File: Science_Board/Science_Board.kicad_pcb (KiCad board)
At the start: 2 copper layers, 217 x 149.5 mm, 136 parts, among them J1 Conn_01x02, J10 Conn_01x02, J11 Conn_01x03, J12 Conn_01x03, J13 Conn_01x03, J14 Conn_01x03, J15 Conn_01x03, J16 Conn_01x03, J17 Conn_01x03, J18 Conn_01x03, J19 Conn_01x02, J2 RJ45_LED_Shielded, J20 Molex_Megafit_02, J21 Molex_Megafit_02, J22 Molex_Megafit_02, J23 Conn_01x02, J3 Molex_Megafit_02, J4 Molex_Megafit_02, J5 Conn_01x05, J6 Conn_01x04, J7 Conn_01x03, J8 Conn_01x03, J9 Conn_01x02, Q1 BS250, Q2 NMOS, Q3 NMOS, Q4 NMOS, Q5 NMOS, SW1 SW_Push, SW10 SW_Push, SW11 SW_Push, SW12 SW_SPDT, SW2 SW_Push, SW3 SW_Push, SW4 SW_Push, SW5 SW_Push, SW6 SW_Push, SW7 SW_Push, SW8 SW_Push, SW9 SW_Push, U1 AP63205WU, U5 PCA9685BS

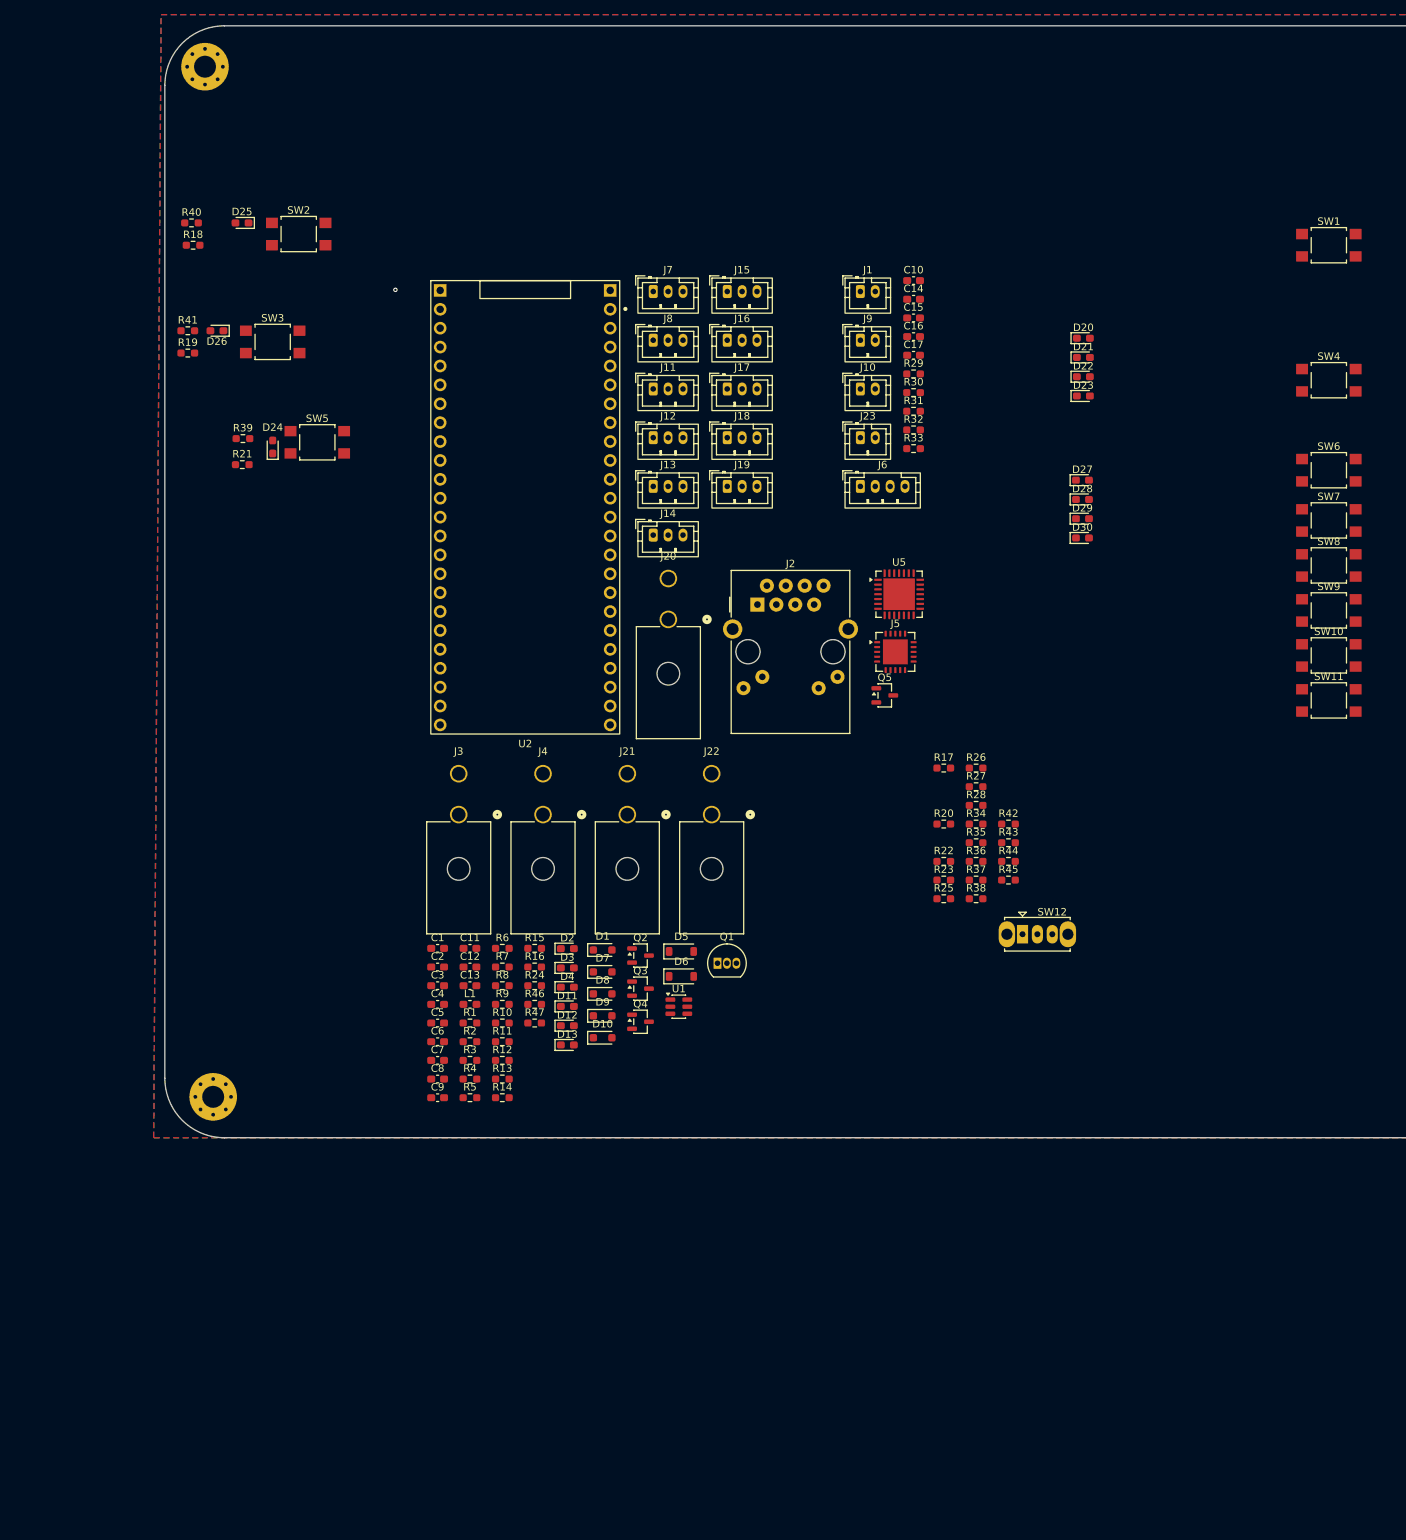
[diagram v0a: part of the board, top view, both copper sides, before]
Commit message: Got all the buttons close to eachother
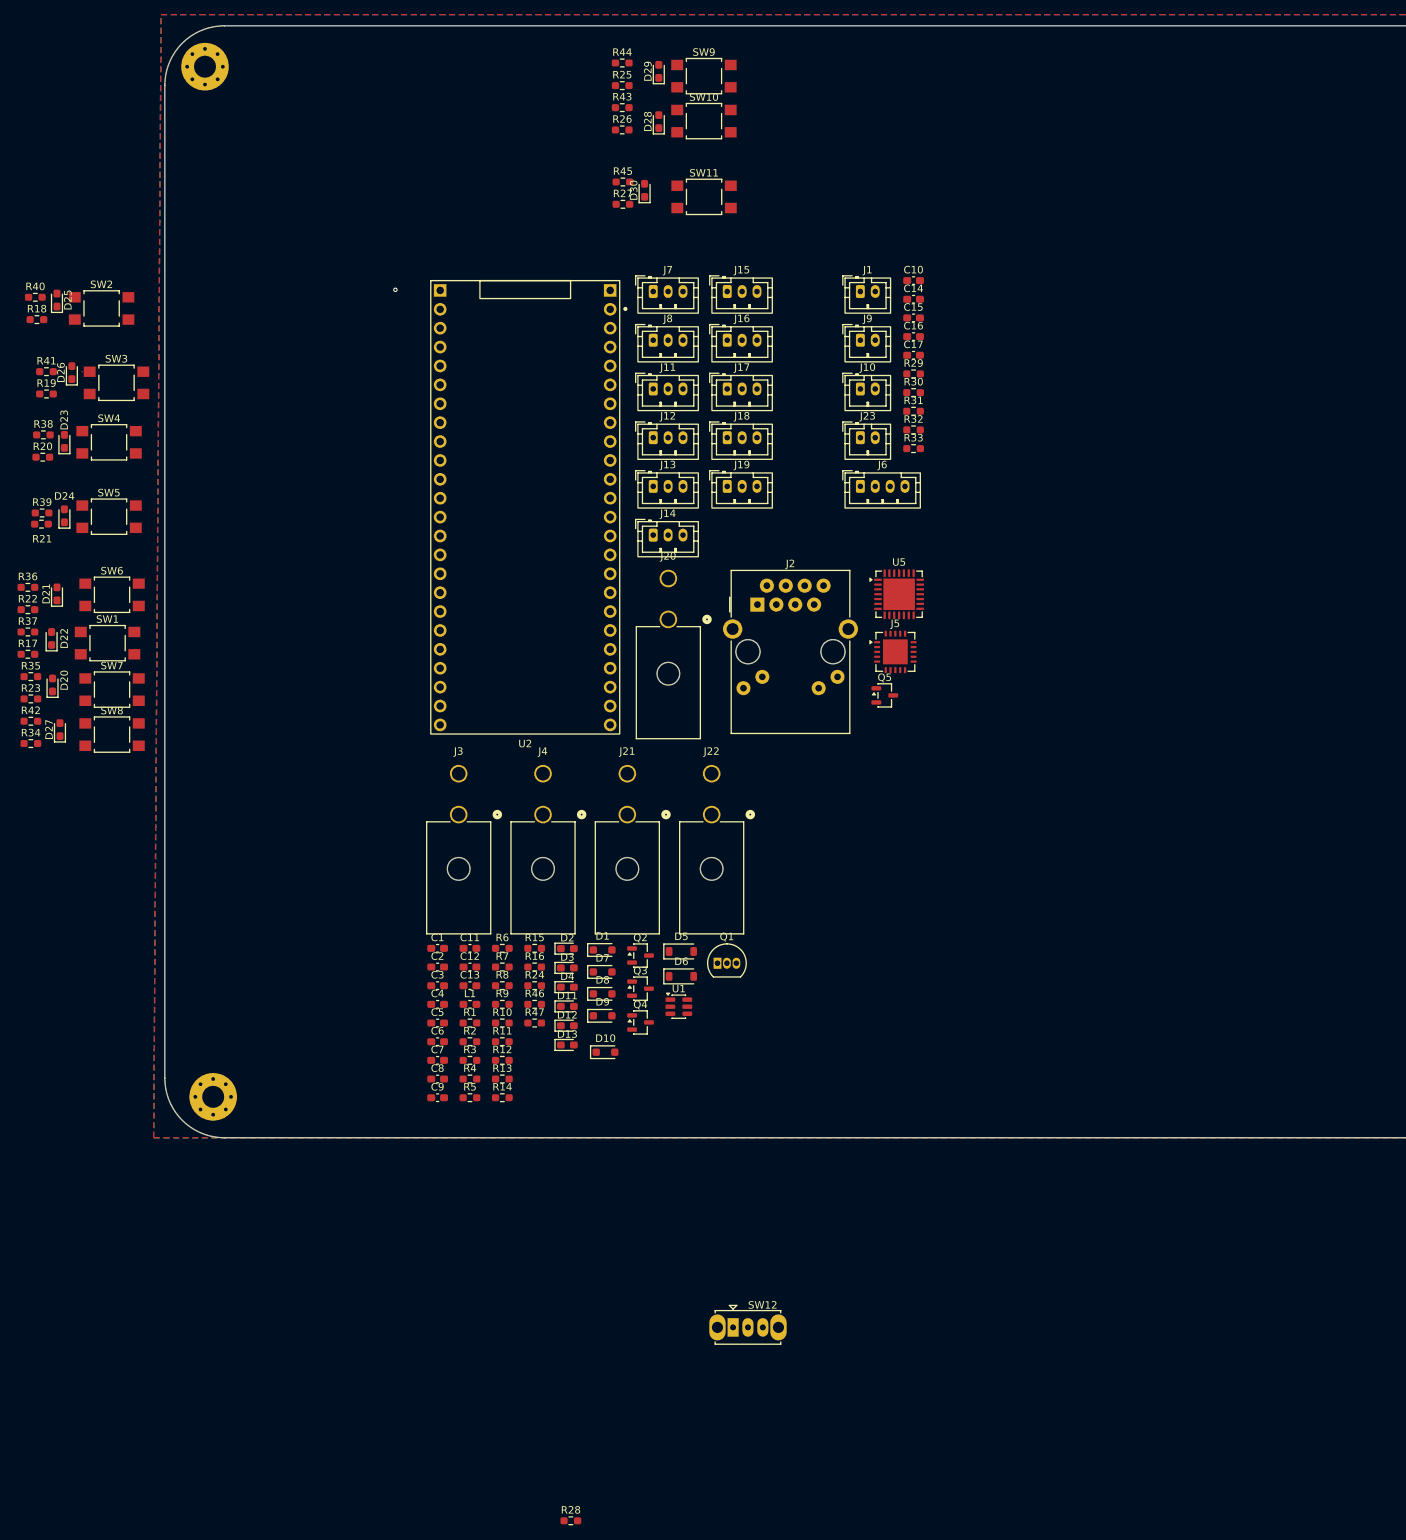
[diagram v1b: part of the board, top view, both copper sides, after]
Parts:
- moved SW1 172.7 mm to (22.8, 98.0)
- moved SW7 165.2 mm to (23.4, 104.2)
- moved SW8 165.2 mm to (23.4, 110.3)
- moved SW6 164.5 mm to (23.4, 91.5)
- moved SW4 164.2 mm to (23.0, 71.0)
- moved D20 146.2 mm to (15.4, 103.6), turned to 90 degrees
- moved D22 143.1 mm to (15.3, 97.4), turned to 90 degrees
- moved D21 141.6 mm to (16.0, 91.4), turned to 90 degrees
- moved D27 141.5 mm to (16.4, 109.6), turned to 90 degrees
- moved R38 140.1 mm to (14.2, 70.0)
- moved D23 137.1 mm to (17.0, 70.9), turned to 90 degrees
- moved R36 132.7 mm to (12.1, 90.5)
- moved R42 132.2 mm to (12.5, 108.5)
- moved R37 131.8 mm to (12.1, 96.5)
- moved R20 130.8 mm to (14.1, 73.0)
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
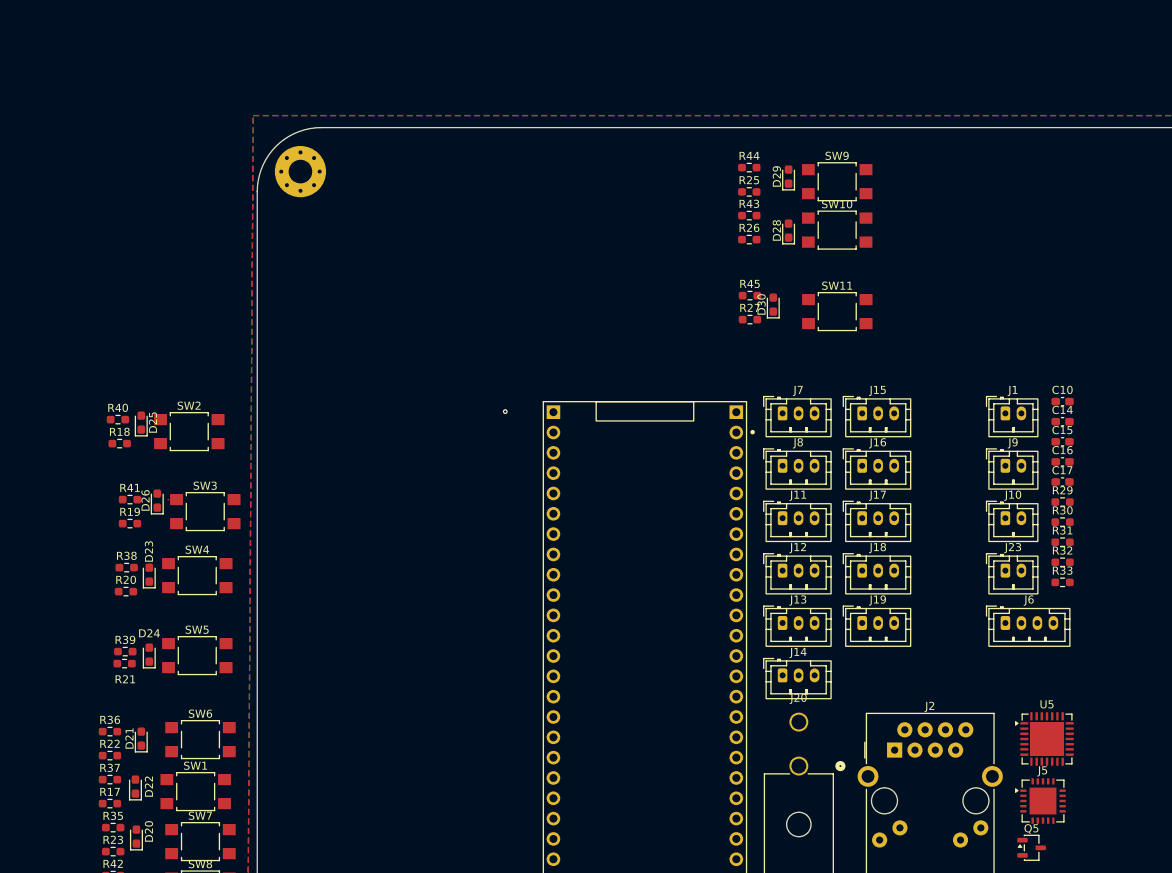
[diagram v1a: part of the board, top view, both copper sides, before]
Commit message: fixed pwm driver and a connecter footprint
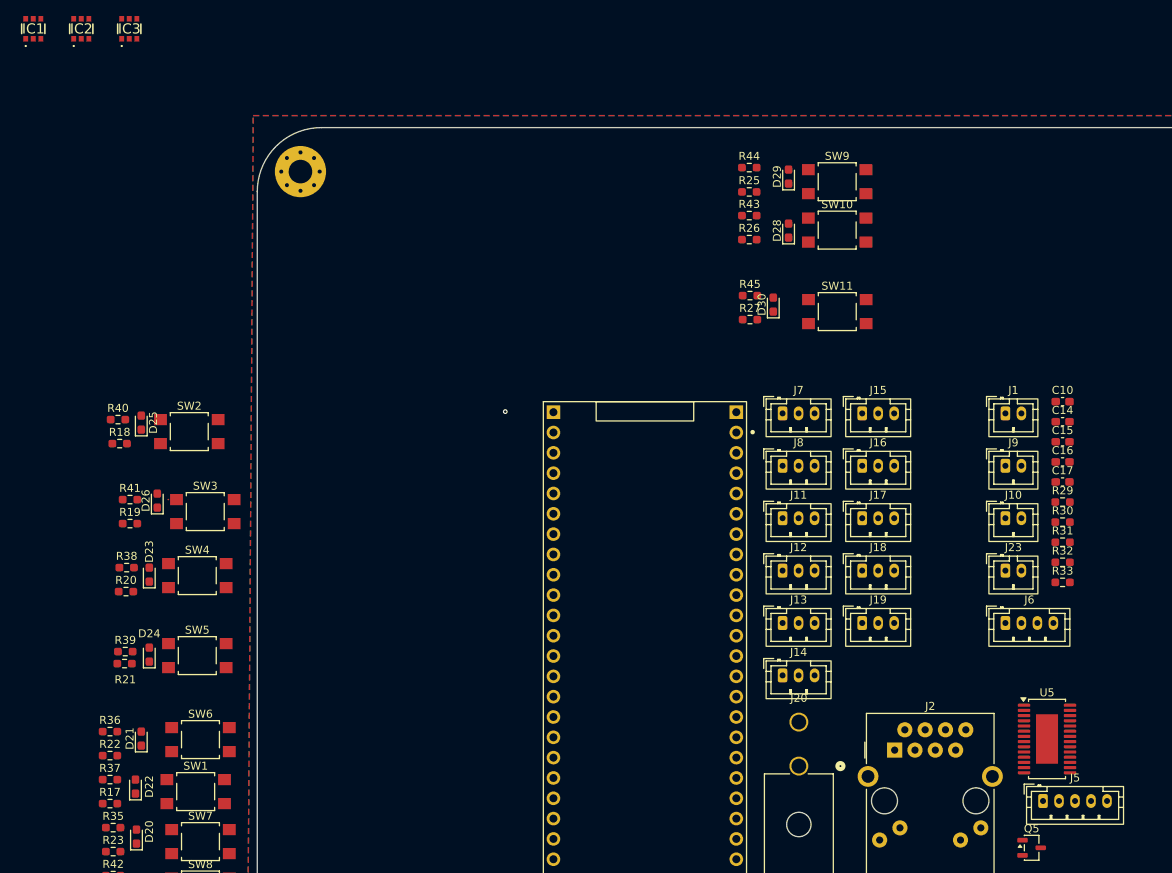
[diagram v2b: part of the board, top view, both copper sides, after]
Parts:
- added IC1: TCKE603RA, MRDT_Devices:TCKE602RM, F.Cu at (2.50, 2.65)
- added IC2: TCKE603RA, MRDT_Devices:TCKE602RM, F.Cu at (8.50, 2.65)
- added IC3: TCKE603RM, MRDT_Devices:TCKE602RM, F.Cu at (14.5, 2.65)
- J5: footprint Package_DFN_QFN:QFN-20-1EP_5x5mm_P0.65mm_EP3.35x3.35mm -> Connector_JST:JST_PH_B5B-PH-K_1x05_P2.00mm_Vertical
- U5: value PCA9685BS -> PCA9685PW; footprint Package_DFN_QFN:QFN-28-1EP_6x6mm_P0.65mm_EP4.25x4.25mm -> Package_SO:HTSSOP-28-1EP_4.4x9.7mm_P0.65mm_EP2.75x6.2mm

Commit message: moved stuff off board
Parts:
- moved L1 203.0 mm to (265.4, 86.4)
- moved C11 201.7 mm to (265.4, 83.6)
- moved C1 201.7 mm to (261.1, 83.6)
- moved C2 201.7 mm to (261.1, 86.1)
- moved C3 201.7 mm to (261.1, 88.6)
- moved R1 185.7 mm to (255.6, 124.5)
- moved J7 184.5 mm to (270.3, -10.2)
- moved C12 179.7 mm to (250.2, 121.7)
- moved C13 179.7 mm to (250.2, 124.2)
- moved U1 175.0 mm to (265.3, 90.5)
- moved D1 166.8 mm to (255.3, 121.9)
- moved J8 163.3 mm to (252.5, 10.2)
- moved J2 158.5 mm to (259.6, 39.9)
- moved Q1 156.7 mm to (260.4, 121.9)
- moved C10 146.1 mm to (276.9, 38.1)
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
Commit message: fixed the 1wire pin
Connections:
- U2 pad 12: unconnected-(U2-PA8-Pad12) -> AF_EN
- U2 pad 17: AF_EN -> 1_WIRE
- U2 pad 35: 1_WIRE -> unconnected-(U2-PH1-Pad35)
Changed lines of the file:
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@@
 			(layers "*.Cu" "*.Mask")
 			(remove_unused_layers no)
-			(net "unconnected-(U2-PA8-Pad12)")
+			(net "AF_EN")
 			(pinfunction "PA8_12")
-			(pintype "bidirectional+no_connect")
+			(pintype "bidirectional")
 		)
 		(pad "13" thru_hole circle
@@
 			(layers "*.Cu" "*.Mask")
 			(remove_unused_layers no)
-			(net "AF_EN")
+			(net "1_WIRE")
 			(pinfunction "PB14_17")
 			(pintype "bidirectional")
@@
 			(layers "*.Cu" "*.Mask")
 			(remove_unused_layers no)
-			(net "1_WIRE")
+			(net "unconnected-(U2-PH1-Pad35)")
 			(pinfunction "PH1_35")
-			(pintype "bidirectional")
+			(pintype "bidirectional+no_connect")
 		)
 		(pad "36" thru_hole circle
